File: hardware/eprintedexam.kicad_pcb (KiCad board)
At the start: 2 copper layers, 52.5 x 46.6 mm, 18 parts, among them J1 Conn_01x04, J2 Conn_01x08, SW1 SW_Push, SW2 SW_Push, U1 ESP-12F

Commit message: updated hardware diagram and added woking epd4in2b_v2 driver
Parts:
- moved R4 4.05 mm to (111.8, 61.9), turned to 0 degrees
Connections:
- J2 pad 3: /din -> /cs
- J2 pad 4: /clk -> /dc
- J2 pad 5: /cs -> /rst
- J2 pad 6: /dc -> /busy
- J2 pad 7: /rst -> /mosi
- J2 pad 8: /busy -> /clk
- R3 pad 2: Net-(R3-Pad2) -> /rst
- R4 pad 2: Net-(R4-Pad2) -> /busy
- SW1 pad 2: Net-(R3-Pad2) -> /rst
- TP1 pad 1: /cs -> /rst
- TP2 pad 1: /dc -> /busy
- TP3 pad 1: /clk -> /dc
- TP4 pad 1: /din -> /cs
- TP5 pad 1: /busy -> /clk
- TP6 pad 1: /rst -> /mosi
- U1 pad 11: /dc -> Net-(U1-Pad11)
- U1 pad 13: /clk -> Net-(U1-Pad13)
- U1 pad 14: /din -> Net-(U1-Pad14)
- U1 pad 16: Net-(R4-Pad2) -> /busy
- U1 pad 18: Net-(R3-Pad2) -> /rst
- U1 pad 19: Net-(U1-Pad19) -> /cs
- U1 pad 20: Net-(U1-Pad20) -> /dc
- U1 pad 4: /busy -> Net-(U1-Pad4)
- U1 pad 5: /rst -> /clk
- U1 pad 7: Net-(U1-Pad7) -> /mosi
- U1 pad 9: /cs -> Net-(U1-Pad9)
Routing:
- net /mosi: track 0.00 -> 37.1 mm
- net /din: track 22.7 -> 0.00 mm
- net /clk: track 21.8 -> 42.6 mm
- net /cs: track 27.7 -> 8.40 mm, vias 2 -> 0
- net Net-(R3-Pad2): track 19.3 -> 0.00 mm
- net /busy: track 43.4 -> 27.3 mm
- net /rst: track 40.1 -> 26.4 mm
- net /dc: track 21.0 -> 7.79 mm
- net Net-(R4-Pad2): track 6.62 -> 0.00 mm

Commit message: mayor hardware revision
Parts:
- removed R1: 10k, Resistor_SMD:R_1206_3216Metric
- removed R5: R, Resistor_SMD:R_1206_3216Metric
- removed TP7, TP8: TestPoint, TestPoint:TestPoint_Pad_D1.5mm
- added BT1: Battery_Cell, Battery:BatteryHolder_MPD_BH-18650-PC2, B.Cu at (107.2, 56.3)
- added C1: 100n, Capacitor_SMD:C_1206_3216Metric, F.Cu at (127.0, 53.5)
- added C2: 100n, Capacitor_SMD:C_1206_3216Metric, F.Cu at (127.0, 61.5)
- added C3: 100n, Capacitor_SMD:C_1206_3216Metric, F.Cu at (158.4, 90.6)
- added C4: 100n, Capacitor_SMD:C_1206_3216Metric, F.Cu at (138.4, 91.6)
- added C5: 100n, Capacitor_SMD:C_1206_3216Metric, F.Cu at (172.7, 86.8)
- added C6: 10n, Capacitor_SMD:C_1206_3216Metric, F.Cu at (169.1, 77.8)
- added C7: 100n, Capacitor_SMD:C_1206_3216Metric, F.Cu at (117.0, 98.4)
- added D1: D, Diode_THT:D_DO-35_SOD27_P10.16mm_Horizontal, B.Cu at (171.1, 101.8)
- added H1: MountingHole, MountingHole:MountingHole_3mm, F.Cu at (94.3, 49.1)
- added H2: MountingHole, MountingHole:MountingHole_3mm, F.Cu at (94.3, 121.6)
- added H3: MountingHole, MountingHole:MountingHole_3mm, F.Cu at (191.3, 49.1)
- added H4: MountingHole, MountingHole:MountingHole_3mm, F.Cu at (191.3, 121.6)
- added Q1: 2N7002, Package_TO_SOT_SMD:SOT-23, F.Cu at (151.9, 91.0)
- added Q2: 2N7002, Package_TO_SOT_SMD:SOT-23, F.Cu at (145.4, 91.0)
- added Q3: 2N7002, Package_TO_SOT_SMD:SOT-23, F.Cu at (148.4, 86.0)
- added Q4: 2N7002, Package_TO_SOT_SMD:SOT-23, F.Cu at (174.3, 81.9)
- added Q5: 2N7002, Package_TO_SOT_SMD:SOT-23, F.Cu at (174.5, 77.3)
- added Q6: AO3401A, Package_TO_SOT_SMD:SOT-23, F.Cu at (111.1, 97.5)
- added R10: 33k, Resistor_SMD:R_1206_3216Metric, F.Cu at (148.4, 97.6)
- added R11: 33k, Resistor_SMD:R_1206_3216Metric, F.Cu at (141.5, 86.0)
- added R12: 10k, Resistor_SMD:R_1206_3216Metric, F.Cu at (175.5, 96.8)
- added R13: 330, Resistor_SMD:R_1206_3216Metric, F.Cu at (169.1, 82.8)
- added R14: 22k, Resistor_SMD:R_1206_3216Metric, F.Cu at (175.5, 91.8)
- added R15: 10k, Resistor_SMD:R_1206_3216Metric, F.Cu at (117.0, 103.2)
- added R16: 10k, Resistor_SMD:R_1206_3216Metric, F.Cu at (111.3, 103.2)
- added R17: 560k, Resistor_SMD:R_1206_3216Metric, F.Cu at (178.5, 86.4)
- added R18: 10k, Resistor_SMD:R_1206_3216Metric, F.Cu at (117.0, 93.8)
- added R6: 1k, Resistor_SMD:R_1206_3216Metric, F.Cu at (158.4, 97.6)
- added R7: 1k, Resistor_SMD:R_1206_3216Metric, F.Cu at (138.4, 97.6)
- added R8: 10k, Resistor_SMD:R_1206_3216Metric, F.Cu at (153.4, 97.6)
- added R9: 10k, Resistor_SMD:R_1206_3216Metric, F.Cu at (143.4, 97.6)
- added SW3: SW_Push, Button_Switch_SMD:SW_SPST_TL3342, F.Cu at (161.7, 110.6)
- added SW4: SW_Push, Button_Switch_SMD:SW_SPST_TL3342, F.Cu at (129.3, 110.6)
- added U2: ESP-12F, RF_Module:ESP-12E, F.Cu at (144.1, 51.0)
- J2: moved to F.Cu
- U1: value ESP-12F -> AP1117-33; footprint RF_Module:ESP-12E -> Package_TO_SOT_SMD:SOT-223-3_TabPin2
- moved SW2 99.1 mm to (183.9, 65.2), turned to 180 degrees
- moved R3 61.2 mm to (183.2, 59.8), turned to 180 degrees
- moved J1 57.4 mm to (185.5, 55.7)
- moved R2 46.4 mm to (131.1, 53.5), turned to 270 degrees
- moved R4 44.8 mm to (156.2, 67.3), turned to 180 degrees
- moved TP5 36.0 mm to (115.6, 107.4)
- moved U1 28.7 mm to (120.5, 67.7)
- moved TP4 26.3 mm to (93.4, 85.4)
- moved SW1 23.2 mm to (97.4, 57.8), turned to 90 degrees
- moved J2 23.1 mm to (96.9, 72.7), turned to 0 degrees
- moved TP3 21.6 mm to (93.5, 82.8)
- moved TP6 16.8 mm to (93.5, 90.5)
- moved TP1 16.6 mm to (93.5, 77.8)
- moved TP2 13.2 mm to (93.5, 80.3)
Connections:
- J1 pad 3: Net-(J1-Pad3) -> nxt
- J2 pad 3: /cs -> spi-mosi
- J2 pad 4: /dc -> spi-clk
- J2 pad 5: /rst -> spi-cs
- J2 pad 6: /busy -> spi-dc
- J2 pad 7: /mosi -> spi-nrst
- J2 pad 8: /clk -> spi-busy,flash
- R2 pad 1: VCC -> Net-(R2-Pad1)
- R2 pad 2: Net-(R2-Pad2) -> VCC
- R3 pad 2: /rst -> spi-busy,flash
- R4 pad 2: /busy -> spi-cs
- SW1 pad 2: /rst -> nrst
- SW2 pad 2: Net-(R2-Pad2) -> spi-busy,flash
- TP1 pad 1: /rst -> spi-mosi
- TP2 pad 1: /busy -> spi-clk
- TP3 pad 1: /dc -> spi-cs
- TP4 pad 1: /cs -> spi-dc
- TP5 pad 1: /clk -> spi-rst
- TP6 pad 1: /mosi -> spi-busy,flash
- U1 pad 1: Net-(R2-Pad2) -> GND
- U1 pad 2: Net-(U1-Pad2) -> VCC
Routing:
- net nrst: track 0.00 -> 172.7 mm, vias 0 -> 2
- net spi-busy,flash: track 0.00 -> 118.0 mm, vias 0 -> 2
- net nxt: track 0.00 -> 97.6 mm, vias 0 -> 2
- net spi-dc: track 0.00 -> 91.7 mm, vias 0 -> 2
- net VCC: track 134.4 -> 225.5 mm, vias 2 -> 0
- net spi-rst: track 0.00 -> 86.3 mm, vias 0 -> 2
- net spi-cs: track 0.00 -> 85.0 mm, vias 0 -> 2
- net nxt+prv: track 0.00 -> 72.3 mm
- net GND: track 10.6 -> 79.2 mm, vias 2 -> 8
- net spi-clk: track 0.00 -> 66.9 mm, vias 0 -> 2
- net prv: track 0.00 -> 62.6 mm
- net spi-mosi: track 0.00 -> 61.3 mm, vias 0 -> 2
- net Net-(R2-Pad2): track 49.6 -> 0.00 mm
- net /clk: track 42.6 -> 0.00 mm
- net /mosi: track 37.1 -> 0.00 mm
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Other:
- board size 52.5 x 46.6 mm -> 103 x 98.5 mm

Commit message: changed p-mosfet for n-mosfet in signal inversor
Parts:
- Q6: value AO3401A -> 2N7002
- moved R12 53.6 mm to (123.5, 110.0), turned to 90 degrees
- moved D1 52.7 mm to (118.5, 105.6), turned to 0 degrees
- moved R17 51.9 mm to (133.9, 113.0), turned to 0 degrees
- moved R14 50.4 mm to (128.5, 110.0), turned to 90 degrees
- moved TP4 46.1 mm to (139.2, 91.2)
- moved Q4 44.9 mm to (138.4, 108.8), turned to 270 degrees
- moved Q5 44.7 mm to (143.0, 109.0), turned to 90 degrees
- moved C5 44.2 mm to (133.5, 107.2), turned to 90 degrees
- moved TP1 40.7 mm to (129.0, 58.0)
- moved R13 37.8 mm to (136.2, 101.3), turned to 90 degrees
- moved C6 37.0 mm to (142.5, 103.6), turned to 270 degrees
- moved C4 36.1 mm to (168.4, 111.6)
- moved Q3 28.8 mm to (173.5, 100.0)
- moved R10 28.8 mm to (173.5, 111.6)
- moved R11 28.8 mm to (166.6, 100.0)
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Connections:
- Q6 pad 2: spi-nrst -> GND
- Q6 pad 3: VCC -> spi-nrst
- R18 pad 1: GND -> spi-nrst
- R18 pad 2: spi-nrst -> VCC
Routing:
- net VCC: track 225.5 -> 359.2 mm, vias 0 -> 6
- net nrst: track 172.7 -> 132.1 mm, vias 2 -> 1
- net Net-(R7-Pad2): track 19.1 -> 50.6 mm
- net spi-dc: track 91.7 -> 116.9 mm, vias 2 -> 0
- net spi-busy,flash: track 118.0 -> 137.9 mm, vias 2 -> 4
- net Net-(BT1-Pad1): track 24.2 -> 5.85 mm
- net nxt: track 97.6 -> 115.8 mm, vias 2 -> 0
- net Net-(R6-Pad2): track 16.1 -> 33.1 mm
- net GND: track 79.2 -> 63.0 mm, vias 8 -> 12
- net spi-rst: track 86.3 -> 100.6 mm, vias 2 -> 0
- net prv: track 62.6 -> 76.6 mm, vias 0 -> 2
- net spi-cs: track 85.0 -> 94.1 mm, vias 2 -> 0
- net spi-mosi: track 61.3 -> 54.1 mm, vias 2 -> 0
- net spi-clk: track 66.9 -> 73.1 mm
- net nxt+prv: track 72.3 -> 67.1 mm
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
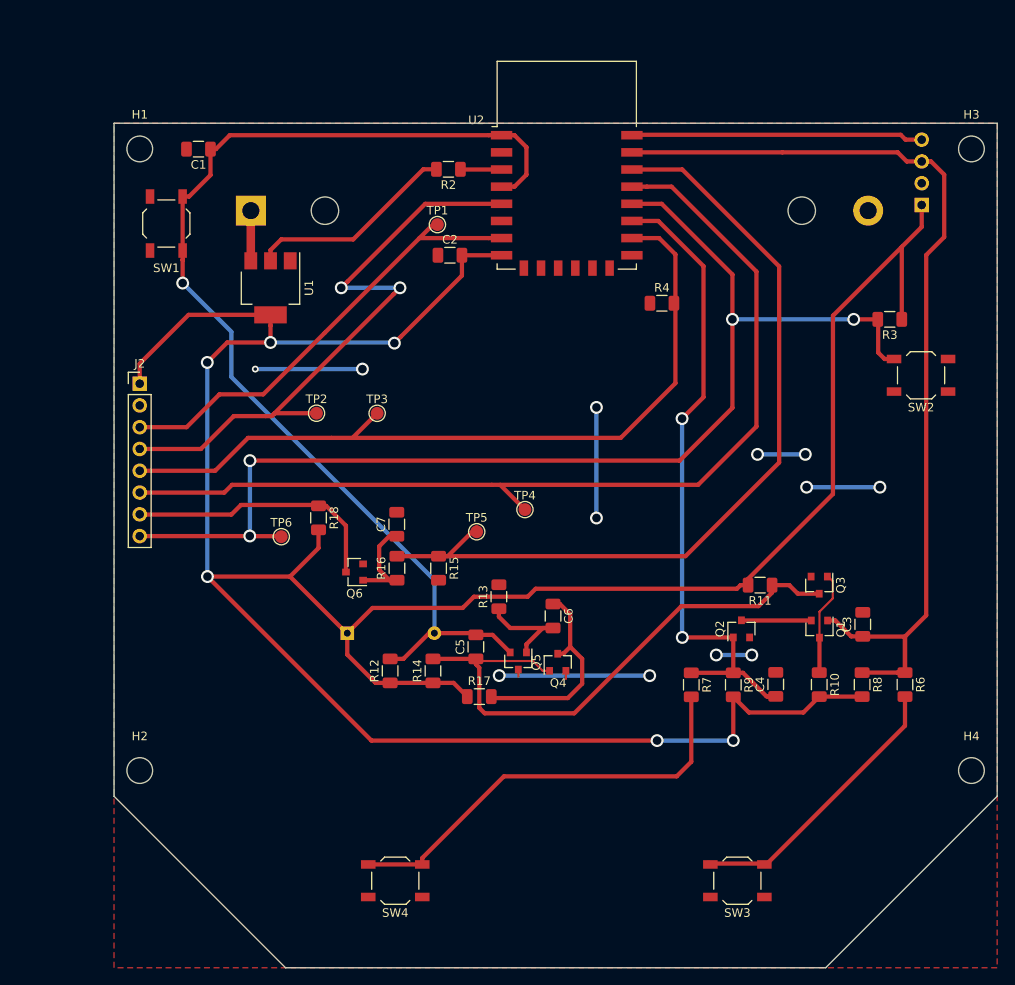
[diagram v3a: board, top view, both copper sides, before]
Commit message: mayor hardware change, fixed bad mosfet connection, increase c6 value to 37uF and decreased R1 to 1k and R10 to 3.3k, and tidy up the pcb desing so fast traces are length minimized
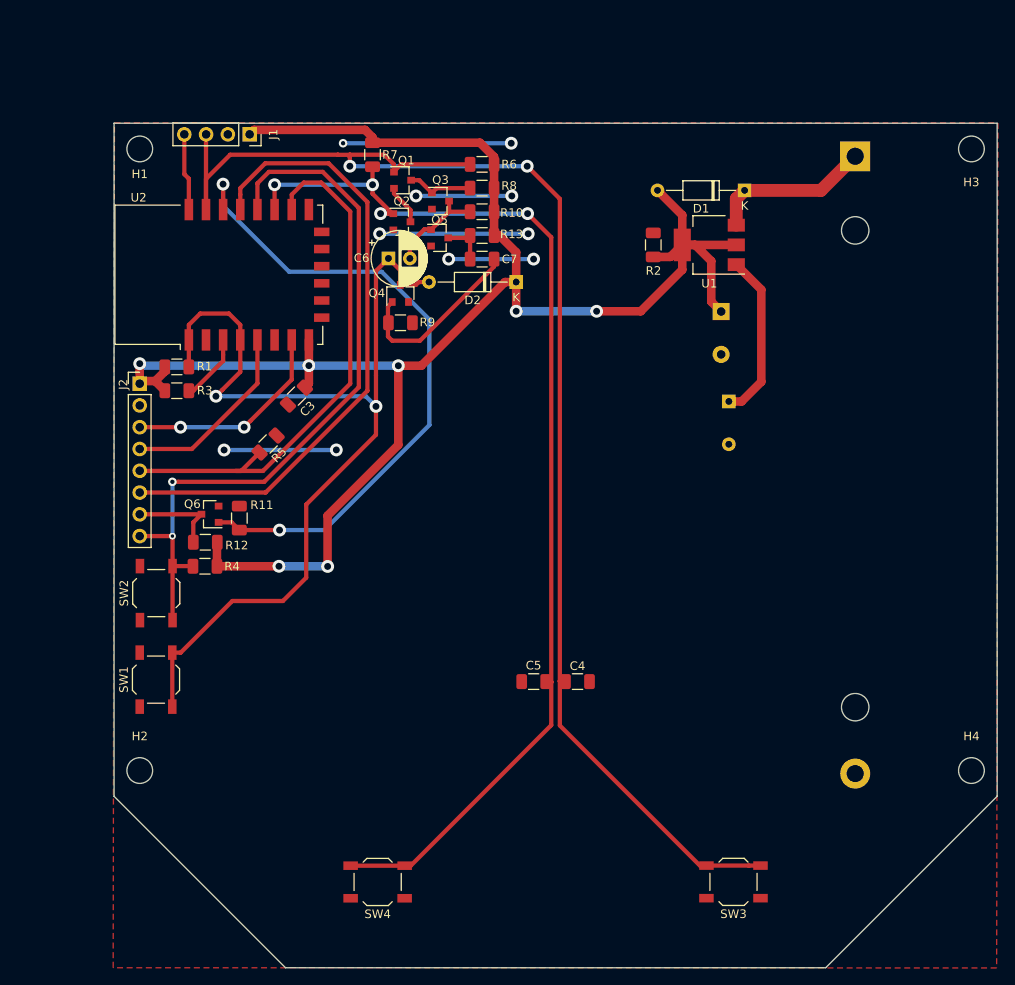
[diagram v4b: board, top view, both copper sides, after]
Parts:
- removed R14: 22k, Resistor_SMD:R_1206_3216Metric
- removed R15, R16, R18: 10k, Resistor_SMD:R_1206_3216Metric
- removed R17: 560k, Resistor_SMD:R_1206_3216Metric
- removed TP1, TP2, TP3, TP4, TP5, TP6: TestPoint, TestPoint:TestPoint_Pad_D1.5mm
- added D2: 2N7001, Diode_THT:D_DO-35_SOD27_P10.16mm_Horizontal, F.Cu at (138.2, 64.7)
- added R1: 1k, Resistor_SMD:R_1206_3216Metric, F.Cu at (98.6, 74.5)
- added R5: 10k, Resistor_SMD:R_1206_3216Metric, F.Cu at (109.2, 83.5)
- C1: value 100n -> 100u; footprint Capacitor_SMD:C_1206_3216Metric -> Capacitor_THT:CP_Radial_D8.0mm_P5.00mm; moved to B.Cu
- C2: value 100n -> 220u; footprint Capacitor_SMD:C_1206_3216Metric -> Capacitor_THT:CP_Radial_D10.0mm_P5.00mm; moved to B.Cu
- C6: value 10n -> 47u; footprint Capacitor_SMD:C_1206_3216Metric -> Capacitor_THT:CP_Radial_D6.3mm_P2.50mm
- D1: value D -> 2N7001; moved to F.Cu
- J1: moved to F.Cu
- R10: value 33k -> 3.3k
- R11: value 33k -> 10k
- R13: value 330 -> 680k
- R2, R8: value 10k -> 33k
- R6, R7: value 1k -> 10k
- R9: value 10k -> 330
- moved SW2 92.7 mm to (96.2, 100.9), turned to 90 degrees
- moved R3 83.6 mm to (98.6, 77.3)
- moved J1 78.8 mm to (107.1, 47.4), turned to 270 degrees
- moved R6 78.2 mm to (134.2, 50.9), turned to 0 degrees
- moved R8 72.9 mm to (134.2, 53.7), turned to 0 degrees
- moved R7 72.1 mm to (121.4, 49.8), turned to 90 degrees
- moved Q1 71.4 mm to (124.9, 52.8), turned to 0 degrees
- moved C3 71.2 mm to (112.5, 78.0), turned to 45 degrees
- moved BT1 70.8 mm to (177.7, 50.0), turned to 270 degrees
- moved D1 69.4 mm to (164.8, 54.0), turned to 180 degrees
- moved C1 68.5 mm to (163.0, 78.6), turned to 270 degrees
- moved R10 67.7 mm to (134.2, 56.5), turned to 180 degrees
- moved Q3 62.9 mm to (129.3, 55.2), turned to 0 degrees
- moved Q2 61.8 mm to (124.8, 57.6), turned to 0 degrees
- moved R4 61.5 mm to (101.9, 97.8), turned to 180 degrees
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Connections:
- C1 pad 1: nrst -> Net-(C1-Pad1)
- C2 pad 1: GND -> VCC
- C2 pad 2: VCC -> GND
- C3 pad 1: nxt -> GND
- C3 pad 2: GND -> VCC
- C4 pad 1: prv -> nxt
- C5 pad 1: nxt+prv -> prv
- C5 pad 2: nrst -> GND
- C6 pad 1: Net-(C6-Pad1) -> nrst
- C6 pad 2: Net-(C6-Pad2) -> nxt+prv
- C7 pad 2: GND -> Net-(C7-Pad2)
- D1 pad 1: VCC -> Net-(BT1-Pad1)
- D1 pad 2: nrst -> VCC
- Q4 pad 1: Net-(C6-Pad2) -> Net-(C7-Pad2)
- Q4 pad 2: nrst -> GND
- Q4 pad 3: GND -> nrst
- Q5 pad 3: Net-(C6-Pad1) -> Net-(C7-Pad1)
- Q6 pad 1: Net-(C7-Pad1) -> spi-rst
- R10 pad 1: Net-(Q1-Pad3) -> VCC
- R10 pad 2: VCC -> nxt+prv
- R11 pad 1: nxt+prv -> spi-rst
- R11 pad 2: VCC -> GND
- R12 pad 2: nrst -> spi-nrst
- R13 pad 1: Net-(C6-Pad2) -> VCC
- R13 pad 2: GND -> Net-(C7-Pad1)
- R2 pad 1: Net-(R2-Pad1) -> VCC
- R2 pad 2: VCC -> GND
- R3 pad 1: VCC -> Net-(R3-Pad1)
- R3 pad 2: spi-busy,flash -> VCC
- R4 pad 1: GND -> VCC
- R4 pad 2: spi-cs -> spi-busy,flash
- R6 pad 2: Net-(R6-Pad2) -> VCC
- R7 pad 2: Net-(R7-Pad2) -> VCC
- R8 pad 1: nxt -> Net-(Q1-Pad3)
- R9 pad 1: prv -> Net-(C7-Pad2)
- R9 pad 2: VCC -> GND
- SW3 pad 2: Net-(R6-Pad2) -> nxt
- SW4 pad 2: Net-(R7-Pad2) -> prv
- U1 pad 1: GND -> Net-(C1-Pad1)
- U2 pad 3: Net-(R2-Pad1) -> Net-(R3-Pad1)
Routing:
- net VCC: track 359.2 -> 206.9 mm, vias 6 -> 7
- net nxt+prv: track 67.1 -> 11.6 mm
- net prv: track 76.6 -> 131.2 mm, vias 2 -> 4
- net spi-clk: track 73.1 -> 22.0 mm, vias 2 -> 0
- net spi-busy,flash: track 137.9 -> 86.8 mm, vias 4 -> 2
- net Net-(R7-Pad2): track 50.6 -> 0.00 mm
- net nxt: track 115.8 -> 165.7 mm, vias 0 -> 2
- net spi-dc: track 116.9 -> 73.9 mm
- net Net-(R6-Pad2): track 33.1 -> 0.00 mm
- net spi-cs: track 94.1 -> 63.1 mm
- net spi-mosi: track 54.1 -> 24.7 mm, vias 0 -> 2
- net Net-(J1-Pad4): track 34.1 -> 8.89 mm
- net Net-(C6-Pad1): track 24.3 -> 0.00 mm
- net spi-rst: track 100.6 -> 77.4 mm, vias 0 -> 2
- net Net-(C7-Pad2): track 0.00 -> 21.3 mm
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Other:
- net class Default: clearance 0.2 -> 0.5; trace_width 0.25 -> 0.5; via_dia 0.8 -> 1.5; via_drill 0.4 -> 0.8
- rule trace_clearance: 0.2 -> 0.5
